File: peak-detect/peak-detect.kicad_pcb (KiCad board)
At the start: 2 copper layers, 53 parts, among them J1 CONN_02X05, J2 CONN_01X03, J3 CONN_01X03, J4 CONN_01X03, J5 CONN_01X03, Q1 BC847, Q2 BC847, U1 LM358, U2 LM358

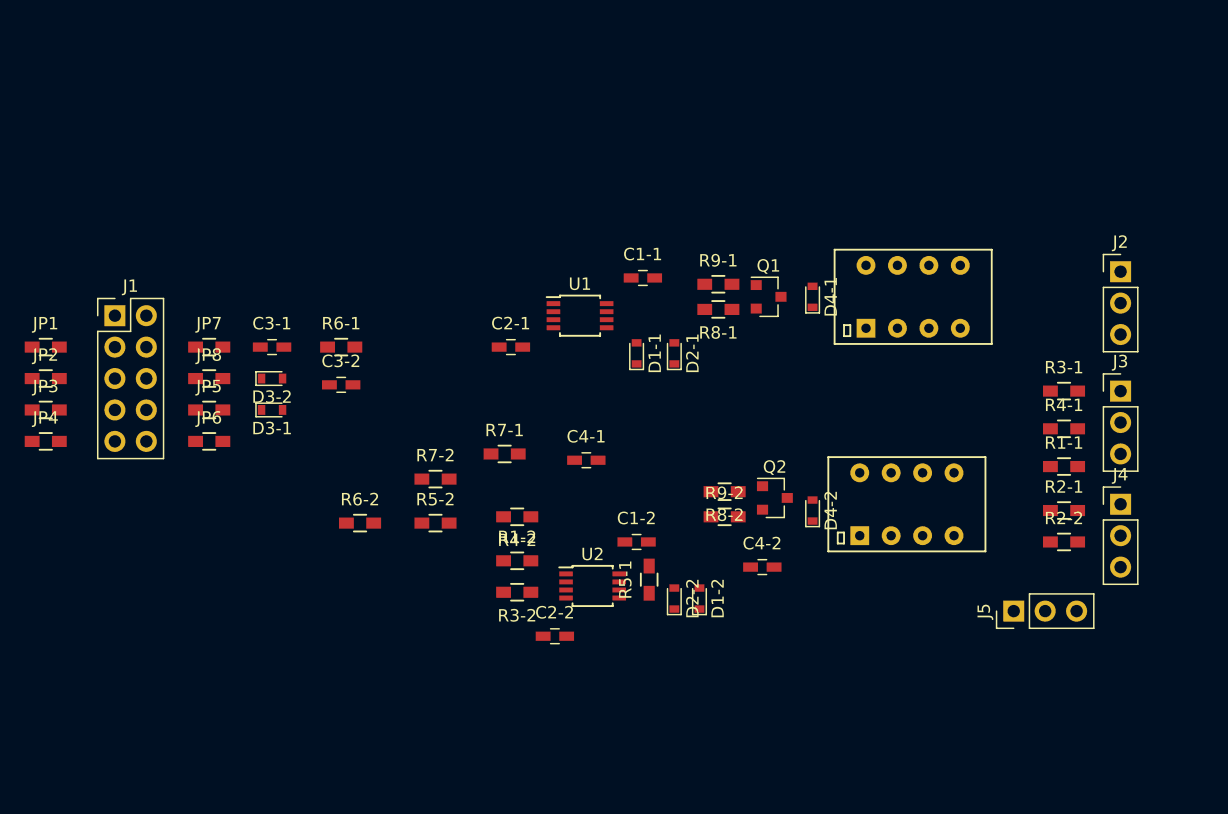
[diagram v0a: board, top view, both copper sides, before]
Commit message: Added virtual ground mixer.
Back wiring and front placement.
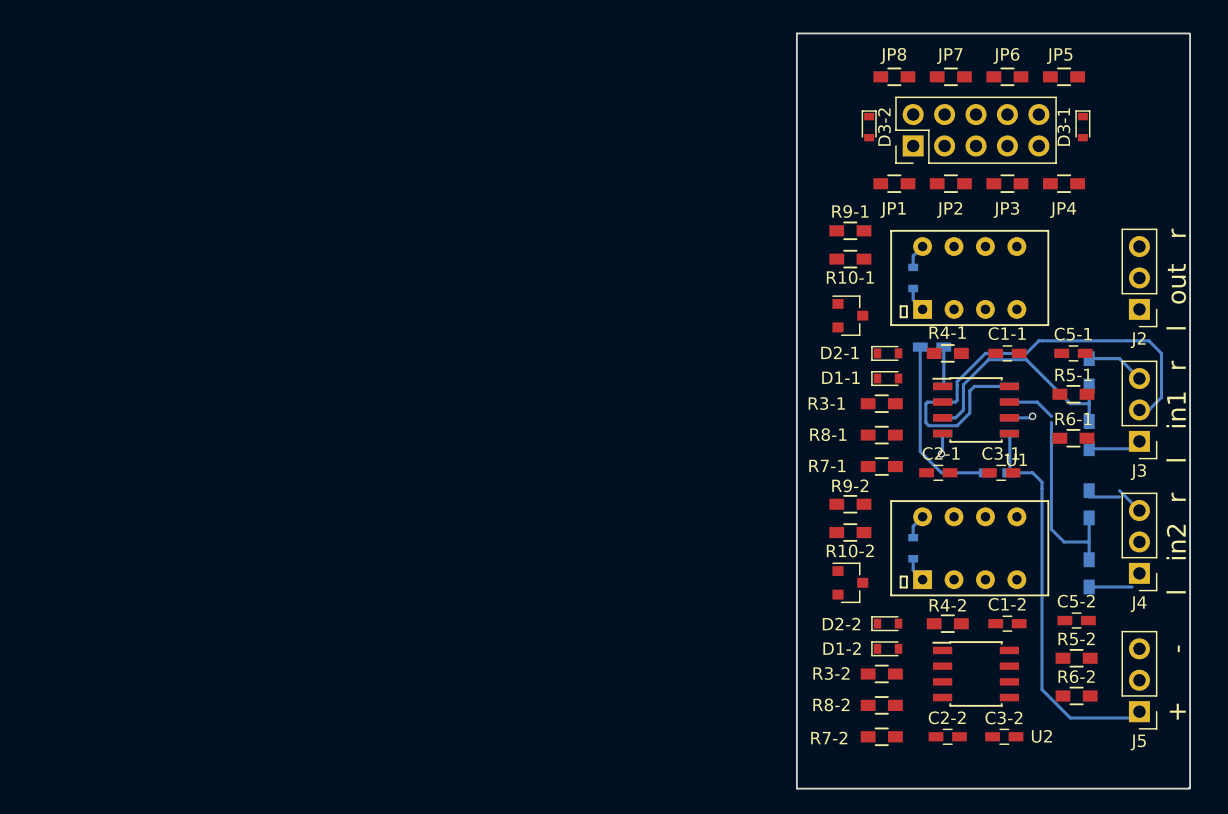
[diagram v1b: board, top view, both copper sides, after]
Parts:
- removed C4-1, C4-2: 1uF, Capacitors_SMD:C_0603_HandSoldering
- added C1: 100nF, Capacitors_SMD:C_0603_HandSoldering, B.Cu at (168.7, 74.2)
- added C2: 100nF, Capacitors_SMD:C_0603_HandSoldering, B.Cu at (174.0, 84.3)
- added C5-1: 1uF, Capacitors_SMD:C_0603_HandSoldering, F.Cu at (180.1, 74.7)
- added C5-2: 1uF, Capacitors_SMD:C_0603_HandSoldering, F.Cu at (180.3, 96.3)
- added R10-1: 1k, Resistors_SMD:R_0603_HandSoldering, F.Cu at (162.1, 67.1)
- added R10-2: 1k, Resistors_SMD:R_0603_HandSoldering, F.Cu at (162.1, 89.2)
- added U3: OPA2134, Housings_SOIC:SOIC-8_3.9x4.9mm_Pitch1.27mm, B.Cu at (172.2, 79.2)
- D4-1, D4-2, R1-1, R1-2, R2-1, R2-2: moved to B.Cu
- R7-1, R7-2: value 1k -> 10k
- U1, U2: footprint Housings_SSOP:TSSOP-8_3x3mm_Pitch0.65mm -> Housings_SOIC:SOIC-8_3.9x4.9mm_Pitch1.27mm
- moved JP4 84.9 mm to (179.3, 61.0)
- moved JP3 79.8 mm to (174.8, 61.0)
- moved JP2 74.8 mm to (170.2, 61.0)
- moved JP5 74.1 mm to (179.3, 52.3), turned to 180 degrees
- moved JP6 70.9 mm to (174.8, 52.3), turned to 180 degrees
- moved JP1 69.8 mm to (165.6, 61.0)
- moved D3-1 69.4 mm to (180.8, 56.4), turned to 270 degrees
- moved J1 66.0 mm to (167.1, 57.9), turned to 90 degrees
- moved JP7 63.8 mm to (170.2, 52.3), turned to 180 degrees
- moved C3-2 60.7 mm to (174.5, 105.7)
- moved JP8 60.5 mm to (165.6, 52.3), turned to 180 degrees
- moved C3-1 59.8 mm to (174.2, 84.3)
- moved R6-1 59.6 mm to (180.1, 81.5), turned to 180 degrees
- moved R6-2 59.6 mm to (180.3, 102.4), turned to 180 degrees
- moved R5-2 53.0 mm to (180.3, 99.3), turned to 180 degrees
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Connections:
- C1-1 pad 1: GND -> GNDD
- C1-2 pad 1: GND -> GNDD
- C2-1 pad 1: GND -> GNDD
- C2-2 pad 1: GND -> GNDD
- J5 pad 2: GND -> GNDD
- R3-1 pad 1: Net-(D1-1-Pad1) -> Net-(R3-1-Pad1)
- R3-2 pad 1: Net-(D1-2-Pad1) -> Net-(R3-2-Pad1)
- R4-1 pad 1: Net-(D2-1-Pad2) -> Net-(D1-1-Pad1)
- R4-1 pad 2: Net-(R1-1-Pad1) -> Net-(R3-1-Pad1)
- R4-2 pad 1: Net-(D2-2-Pad2) -> Net-(D1-2-Pad1)
- R4-2 pad 2: Net-(R1-2-Pad1) -> Net-(R3-2-Pad1)
- R5-1 pad 1: Net-(C3-1-Pad2) -> Net-(D2-1-Pad2)
- R5-1 pad 2: Net-(D2-1-Pad2) -> Net-(R3-1-Pad1)
- R5-2 pad 1: Net-(C3-2-Pad2) -> Net-(D2-2-Pad2)
- R5-2 pad 2: Net-(D2-2-Pad2) -> Net-(R3-2-Pad1)
- R6-1 pad 1: Net-(C3-1-Pad1) -> Net-(C3-1-Pad2)
- R6-1 pad 2: Net-(C3-1-Pad2) -> Net-(D2-1-Pad2)
- R6-2 pad 1: Net-(C3-2-Pad1) -> Net-(C3-2-Pad2)
- R6-2 pad 2: Net-(C3-2-Pad2) -> Net-(D2-2-Pad2)
- R7-1 pad 1: GND -> Net-(C3-1-Pad1)
- R7-1 pad 2: Out-Peak-1 -> Net-(C3-1-Pad2)
- R7-2 pad 1: GND -> Net-(C3-2-Pad1)
- R7-2 pad 2: Out-Peak-2 -> Net-(C3-2-Pad2)
- R8-1 pad 1: Net-(Q1-Pad1) -> GND
- R8-1 pad 2: Relay-1 -> Out-Peak-1
- R8-2 pad 1: Net-(Q2-Pad1) -> GND
- R8-2 pad 2: Relay-2 -> Out-Peak-2
- R9-1 pad 1: GNDD -> Net-(Q1-Pad1)
- R9-1 pad 2: Net-(Q1-Pad1) -> Relay-1
- R9-2 pad 1: GNDD -> Net-(Q2-Pad1)
- R9-2 pad 2: Net-(Q2-Pad1) -> Relay-2
- U1 pad 2: Net-(R1-1-Pad1) -> Net-(R3-1-Pad1)
- U2 pad 2: Net-(R1-2-Pad1) -> Net-(R3-2-Pad1)
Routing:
- net GND: track 0.00 -> 39.0 mm
- net U1+: track 0.00 -> 32.0 mm
- net Net-(R1-1-Pad1): track 0.00 -> 19.3 mm
- net Net-(R1-2-Pad1): track 0.00 -> 18.9 mm
- net GNDD: track 0.00 -> 14.5 mm
- net In-Right-2: track 0.00 -> 4.73 mm
- net In-Right-1: track 0.00 -> 4.73 mm
- net In-Left-2: track 0.00 -> 4.31 mm
- net In-Left-1: track 0.00 -> 4.31 mm
- net +5V: track 0.00 -> 4.01 mm
- net U1-: track 0.00 -> 3.21 mm
- net Net-(D4-2-Pad2): track 0.00 -> 2.01 mm
- net Net-(D4-1-Pad2): track 0.00 -> 2.01 mm
- net Net-(R3-2-Pad1): track 0.00 -> 1.92 mm, vias 0 -> 1
- net Net-(R3-1-Pad1): track 0.00 -> 1.69 mm, vias 0 -> 1
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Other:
- board outline added: 31.8 x 61 mm
- board text added: "+"
- board text added: "-"
- board text added: "in1"
- board text added: "in2"
- board text added: "l"
- board text added: "out"
- board text added: "r"

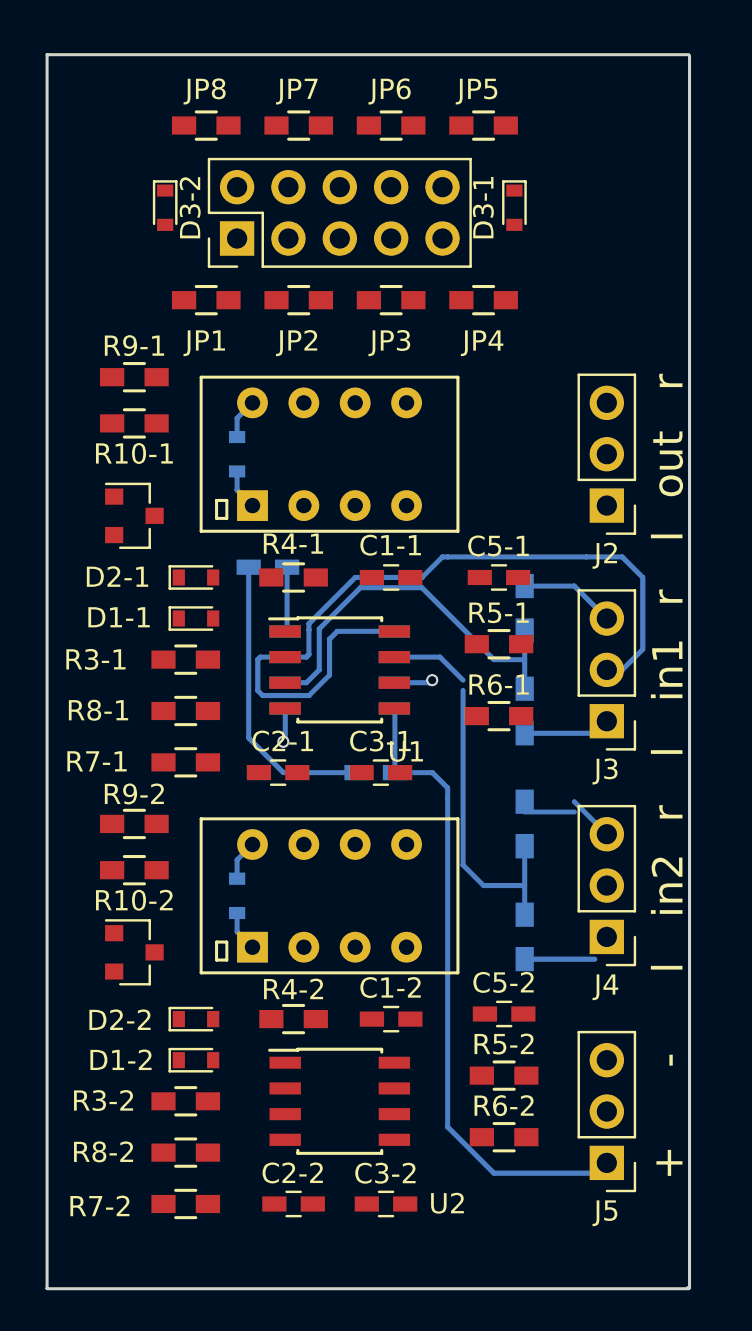
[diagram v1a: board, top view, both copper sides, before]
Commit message: Peak detect routed
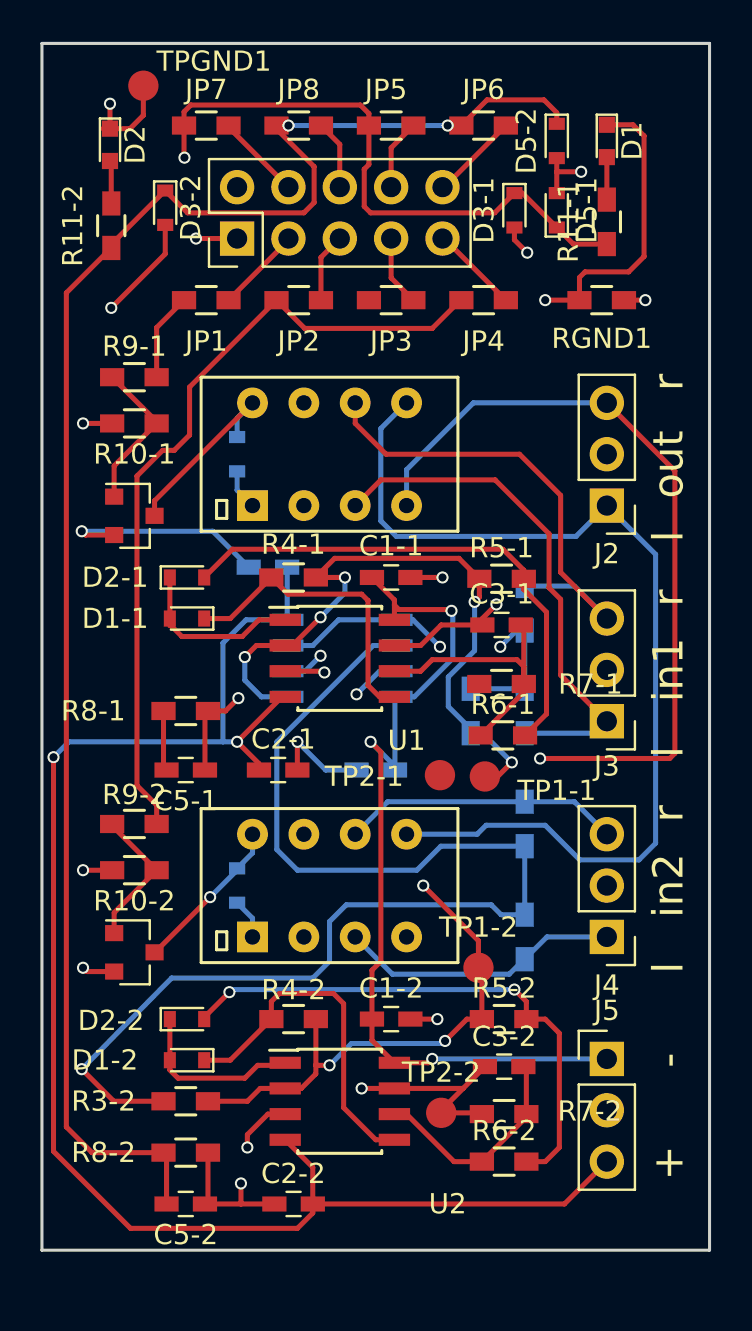
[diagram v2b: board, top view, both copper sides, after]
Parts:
- added D1: LED_Small, LEDs:LED_0603, F.Cu at (185.4, 53.1)
- added D2: LED_Small, LEDs:LED_0603, F.Cu at (160.8, 53.3)
- added D5-1: 5v, Diodes_SMD:D_0603, F.Cu at (182.9, 56.5)
- added D5-2: 5v, Diodes_SMD:D_0603, F.Cu at (182.9, 53.1)
- added R11-1: 1k, Resistors_SMD:R_0603_HandSoldering, F.Cu at (185.4, 57.1)
- added R11-2: 1k, Resistors_SMD:R_0603_HandSoldering, F.Cu at (160.9, 57.3)
- added RGND1: 0, Resistors_SMD:R_0603_HandSoldering, F.Cu at (185.2, 61.0)
- added TP1-1: TEST, Measurement_Points:Measurement_Point_Round-SMD-Pad_Small, F.Cu at (179.4, 84.5)
- added TP1-2: TEST, Measurement_Points:Measurement_Point_Round-SMD-Pad_Small, F.Cu at (179.1, 94.0)
- added TP2-1: TEST, Measurement_Points:Measurement_Point_Round-SMD-Pad_Small, F.Cu at (177.2, 84.5)
- added TP2-2: TEST, Measurement_Points:Measurement_Point_Round-SMD-Pad_Small, F.Cu at (177.2, 101.2)
- added TPGND1: TEST, Measurement_Points:Measurement_Point_Round-SMD-Pad_Small, F.Cu at (162.5, 50.4)
- R3-1: moved to B.Cu
- moved C5-2 18.3 mm to (164.6, 105.7), turned to 180 degrees
- moved C5-1 18.2 mm to (164.6, 84.2), turned to 0 degrees
- moved R7-2 16.4 mm to (180.3, 101.2), turned to 0 degrees
- moved R7-1 16.1 mm to (180.2, 79.9), turned to 0 degrees
- moved R3-1 14.3 mm to (178.7, 81.3), turned to 90 degrees
- moved C3-1 9.43 mm to (180.2, 77.0)
- moved C3-2 8.96 mm to (180.3, 98.9)
- moved J5 5.14 mm to (185.4, 98.5), turned to 0 degrees
- moved JP5 4.57 mm to (174.8, 52.3)
- moved JP6 4.57 mm to (179.3, 52.3)
- moved JP7 4.57 mm to (165.6, 52.3)
- moved JP8 4.57 mm to (170.2, 52.3)
- moved R5-1 3.24 mm to (180.2, 74.7), turned to 180 degrees
- moved R5-2 2.79 mm to (180.3, 96.5)
- moved R6-2 1.21 mm to (180.3, 103.6), turned to 0 degrees
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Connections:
- C5-1 pad 1: GND -> GNDD
- C5-2 pad 1: GND -> GNDD
- J1 pad 1: +5V -> GNDD
- J1 pad 2: GNDD -> +5V
- R8-1 pad 1: GND -> GNDD
- R8-2 pad 1: GND -> GNDD
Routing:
- net Out-Peak-2: track 0.00 -> 84.1 mm, vias 0 -> 2
- net U1-: track 3.21 -> 79.5 mm, vias 0 -> 2
- net Out-Peak-1: track 0.00 -> 65.9 mm, vias 0 -> 2
- net Net-(C3-2-Pad1): track 0.00 -> 61.1 mm, vias 0 -> 2
- net Out-Left: track 0.00 -> 52.2 mm, vias 0 -> 1
- net Out-Right: track 0.00 -> 49.7 mm
- net +5V: track 4.01 -> 49.8 mm
- net GNDD: track 14.5 -> 57.5 mm, vias 0 -> 12
- net Net-(R1-2-Pad1): track 18.9 -> 61.3 mm, vias 0 -> 1
- net Relay-2: track 0.00 -> 39.8 mm
- net Net-(R3-2-Pad1): track 1.92 -> 41.7 mm, vias 1 -> 4
- net Net-(R3-1-Pad1): track 1.69 -> 34.0 mm, vias 1 -> 5
- net Net-(D2-2-Pad2): track 0.00 -> 27.2 mm, vias 0 -> 2
- net Net-(D2-1-Pad2): track 0.00 -> 25.9 mm
- net Net-(C3-1-Pad1): track 0.00 -> 25.6 mm, vias 0 -> 2
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- added copper zone on Gnd, net GND
- added copper zone on Gndd, net GNDD
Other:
- board size 31.8 x 61 mm -> 33 x 59.7 mm
- copper layers 2 -> 4

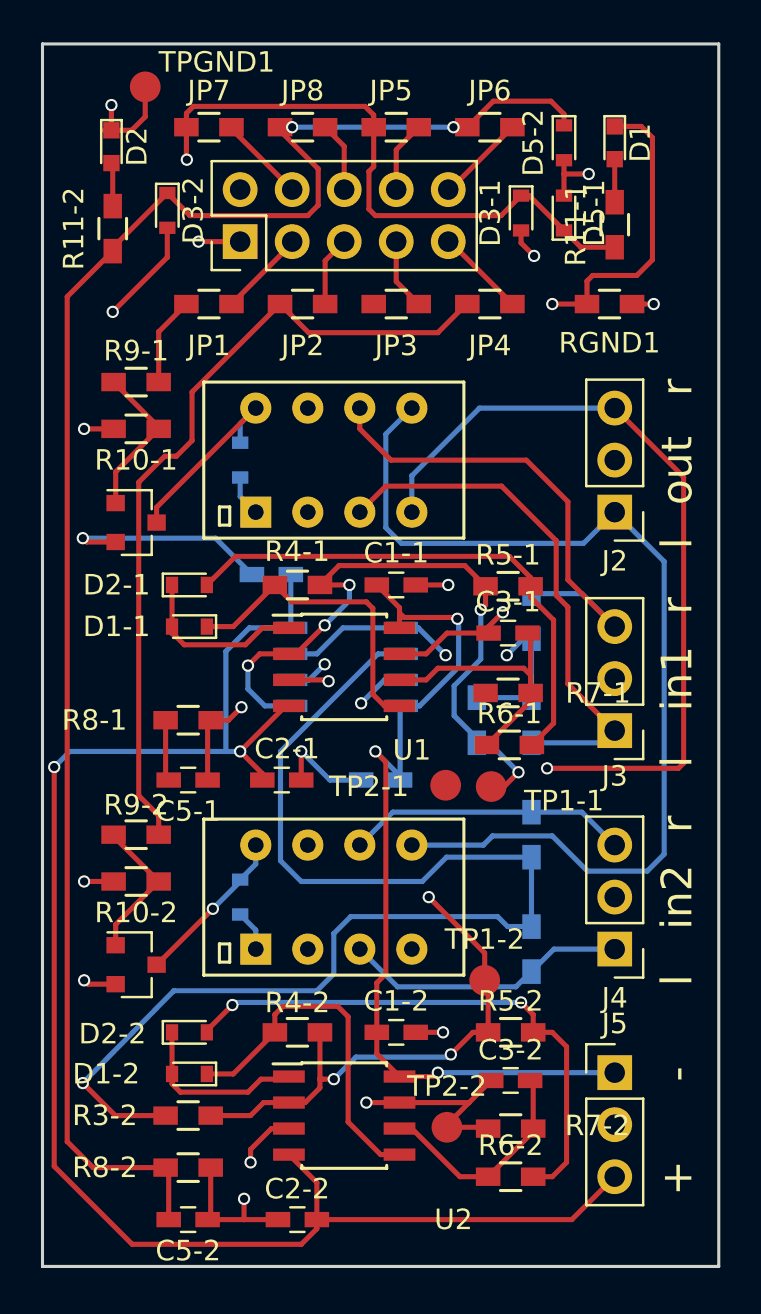
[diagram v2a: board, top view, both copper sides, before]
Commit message: Drill holes, silk screen cleanup
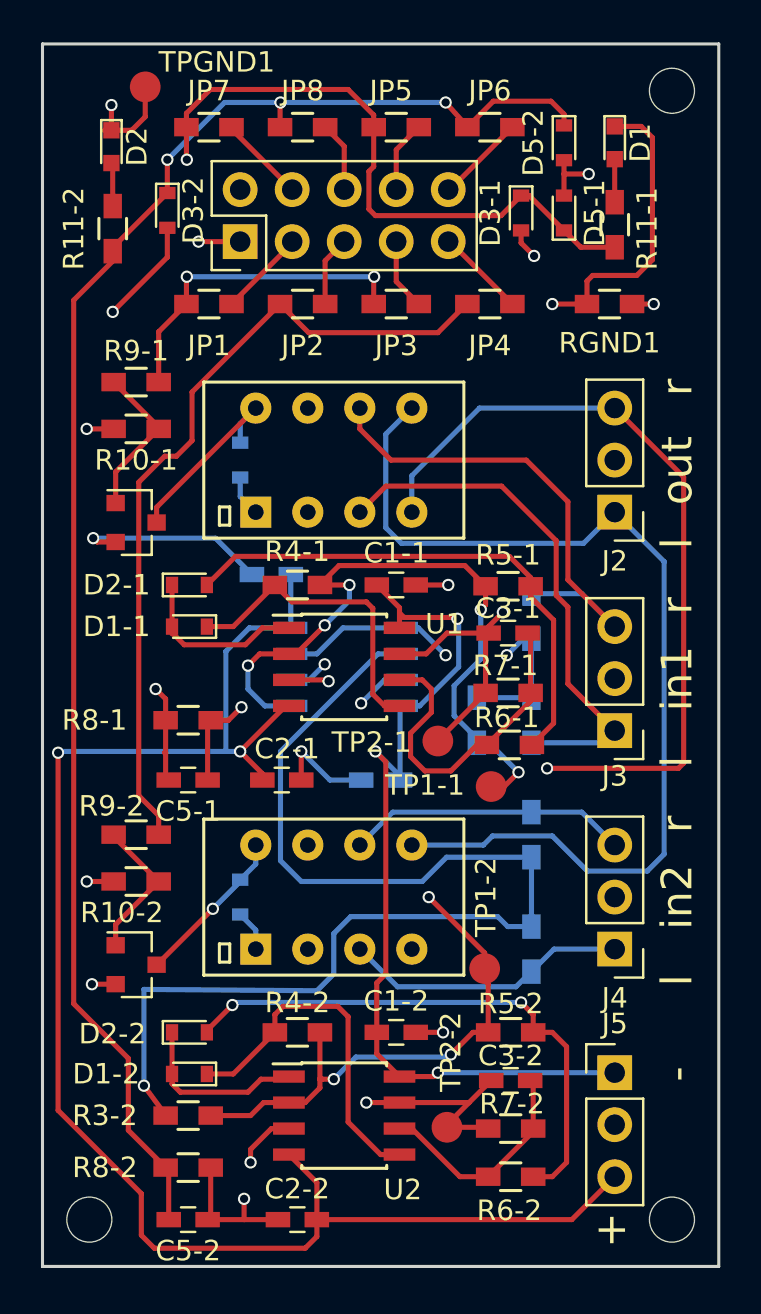
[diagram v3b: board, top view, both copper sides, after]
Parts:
- added REF**: MountingHole_2.2mm_M2_DIN965, Mounting_Holes:MountingHole_2.2mm_M2_DIN965, F.Cu at (188.2, 50.5)
- added REF**: MountingHole_2.2mm_M2_DIN965, Mounting_Holes:MountingHole_2.2mm_M2_DIN965, F.Cu at (159.8, 105.7)
- added REF**: MountingHole_2.2mm_M2_DIN965, Mounting_Holes:MountingHole_2.2mm_M2_DIN965, F.Cu at (188.2, 105.7)
- moved TP2-1 2.19 mm to (176.8, 82.3)
- moved TP1-2 0.57 mm to (179.1, 93.4)
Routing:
- net Relay-1: track 4.37 -> 16.2 mm, vias 0 -> 2
- net Net-(C3-1-Pad1): track 25.6 -> 31.9 mm
- net Out-Peak-2: track 84.1 -> 79.2 mm, vias 2 -> 3
- net Net-(R1-2-Pad1): track 61.3 -> 58.2 mm
- net Net-(C3-1-Pad2): track 14.1 -> 16.4 mm
- net Out-Peak-1: track 65.9 -> 66.6 mm
- net GNDD: track 57.5 -> 57.6 mm, vias 12 -> 13
